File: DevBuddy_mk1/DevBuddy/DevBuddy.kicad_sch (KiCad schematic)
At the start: 5 parts, among them U1 RP2354B

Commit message: Hardware changes, ADC and start of power.
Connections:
- net MUX_S2: now reaches U1.1 (GPIO4)
- net UART_TX_MCU: now reaches U1.77 (GPIO0)
- net UART_RX_MCU: now reaches U1.78 (GPIO1)
- net MUX_S0: now reaches U1.79 (GPIO2)
- net MUX_S1: now reaches U1.80 (GPIO3)
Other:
- added sheet ADC_Channels (ADC_Channels.kicad_sch)
- added sheet Power_Supply_1 (Power_Supply_1.kicad_sch)
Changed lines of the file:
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@@
+	(wire
+		(pts
+			(xy 144.78 71.12) (xy 148.59 71.12)
+		)
+		(stroke
+			(width 0)
+			(type default)
+		)
+	)
 	(wire
 		(pts
@@
 	(wire
 		(pts
+			(xy 144.78 76.2) (xy 148.59 76.2)
+		)
+		(stroke
+			(width 0)
+			(type default)
+		)
+	)
+	(wire
+		(pts
+			(xy 144.78 81.28) (xy 148.59 81.28)
+		)
+		(stroke
+			(width 0)
+			(type default)
+		)
+	)
+	(wire
+		(pts
 			(xy 137.16 45.72) (xy 137.16 46.99)
 		)
@@
 	(wire
 		(pts
+			(xy 144.78 78.74) (xy 148.59 78.74)
+		)
+		(stroke
+			(width 0)
+			(type default)
+		)
+	)
+	(wire
+		(pts
+			(xy 144.78 73.66) (xy 148.59 73.66)
+		)
+		(stroke
+			(width 0)
+			(type default)
+		)
+	)
+	(wire
+		(pts
 			(xy 76.2 44.45) (xy 60.96 44.45)
 		)
@@
 			(width 0)
 			(type default)
+		)
+	)
+	(label "UART_RX_MCU"
+		(at 148.59 73.66 0)
+		(effects
+			(font
+				(size 1.27 1.27)
+			)
+			(justify left bottom)
+		)
+	)
+	(label "UART_TX_MCU"
+		(at 148.59 71.12 0)
+		(effects
+			(font
+				(size 1.27 1.27)
+			)
+			(justify left bottom)
+		)
+	)
+	(global_label "MUX_S1"
+		(shape input)
+		(at 148.59 78.74 0)
+		(fields_autoplaced yes)
+		(effects
+			(font
+				(size 1.27 1.27)
+			)
+			(justify left)
+		)
+		(property "Intersheetrefs" "${INTERSHEET_REFS}"
+			(at 158.9532 78.74 0)
+			(effects
+				(font
+					(size 1.27 1.27)
+				)
+				(justify left)
+				(hide yes)
+			)
+		)
+	)
+	(global_label "MUX_S2"
+		(shape input)
+		(at 148.59 81.28 0)
+		(fields_autoplaced yes)
+		(effects
+			(font
+				(size 1.27 1.27)
+			)
+			(justify left)
+		)
+		(property "Intersheetrefs" "${INTERSHEET_REFS}"
+			(at 158.9532 81.28 0)
+			(effects
+				(font
+					(size 1.27 1.27)
+				)
+				(justify left)
+				(hide yes)
+			)
+		)
+	)
+	(global_label "MUX_S0"
+		(shape input)
+		(at 148.59 76.2 0)
+		(fields_autoplaced yes)
+		(effects
+			(font
+				(size 1.27 1.27)
+			)
+			(justify left)
+		)
+		(property "Intersheetrefs" "${INTERSHEET_REFS}"
+			(at 158.9532 76.2 0)
+			(effects
+				(font
+					(size 1.27 1.27)
+				)
+				(justify left)
+				(hide yes)
+			)
 		)
 	)
@@
 				)
 			)
+		)
+	)
+	(sheet
+		(at 185.42 41.91)
+		(size 57.15 22.86)
+		(exclude_from_sim no)
+		(in_bom yes)
+		(on_board yes)
+		(dnp no)
+		(fields_autoplaced yes)
+		(stroke
+			(width 0.1524)
+			(type solid)
+		)
+		(fill
+			(color 0 0 0 0.0000)
+		)
+		(property "Sheetname" "Power_Supply_1"
+			(at 185.42 41.1984 0)
+			(effects
+				(font
+					(size 1.27 1.27)
+				)
+				(justify left bottom)
+			)
+		)
+		(property "Sheetfile" "Power_Supply_1.kicad_sch"
+			(at 185.42 65.3546 0)
+			(effects
+				(font
+					(size 1.27 1.27)
+				)
+				(justify left top)
+			)
+		)
+		(instances
+			(project "DevBuddy"
+				(path "/cd44a09a-8e2e-49d9-bb56-7efc0bfafbd6"
+					(page "2")
+				)
+			)
+		)
+	)
+	(sheet
+		(at 248.92 41.91)
+		(size 58.42 21.59)
+		(exclude_from_sim no)
+		(in_bom yes)
+		(on_board yes)
+		(dnp no)
+		(fields_autoplaced yes)
+		(stroke
+			(width 0.1524)
+			(type solid)
+		)
+		(fill
+			(color 0 0 0 0.0000)
+		)
+		(property "Sheetname" "ADC_Channels"
+			(at 248.92 41.1984 0)
+			(effects
+				(font
+					(size 1.27 1.27)
+				)
+				(justify left bottom)
+			)
+		)
+		(property "Sheetfile" "ADC_Channels.kicad_sch"
+			(at 248.92 64.0846 0)
+			(effects
+				(font
+					(size 1.27 1.27)
+				)
+				(justify left top)
+			)
+		)
+		(instances
+			(project "DevBuddy"
+				(path "/cd44a09a-8e2e-49d9-bb56-7efc0bfafbd6"
+					(page "3")
+				)
+			)

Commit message: Added mux control, fixed adc tlm control, fixed app, added power in PCB
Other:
- added sheet Power_Supply_2 (Power_Supply_2.kicad_sch)
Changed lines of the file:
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@@
+	)
+	(sheet
+		(at 185.42 73.66)
+		(size 57.15 22.86)
+		(exclude_from_sim no)
+		(in_bom yes)
+		(on_board yes)
+		(dnp no)
+		(fields_autoplaced yes)
+		(stroke
+			(width 0.1524)
+			(type solid)
+		)
+		(fill
+			(color 0 0 0 0.0000)
+		)
+		(property "Sheetname" "Power_Supply_2"
+			(at 185.42 72.9484 0)
+			(effects
+				(font
+					(size 1.27 1.27)
+				)
+				(justify left bottom)
+			)
+		)
+		(property "Sheetfile" "Power_Supply_2.kicad_sch"
+			(at 185.42 97.1046 0)
+			(effects
+				(font
+					(size 1.27 1.27)
+				)
+				(justify left top)
+			)
+		)
+		(instances
+			(project "DevBuddy"
+				(path "/cd44a09a-8e2e-49d9-bb56-7efc0bfafbd6"
+					(page "4")
+				)
+			)
+		)
 	)
 	(sheet

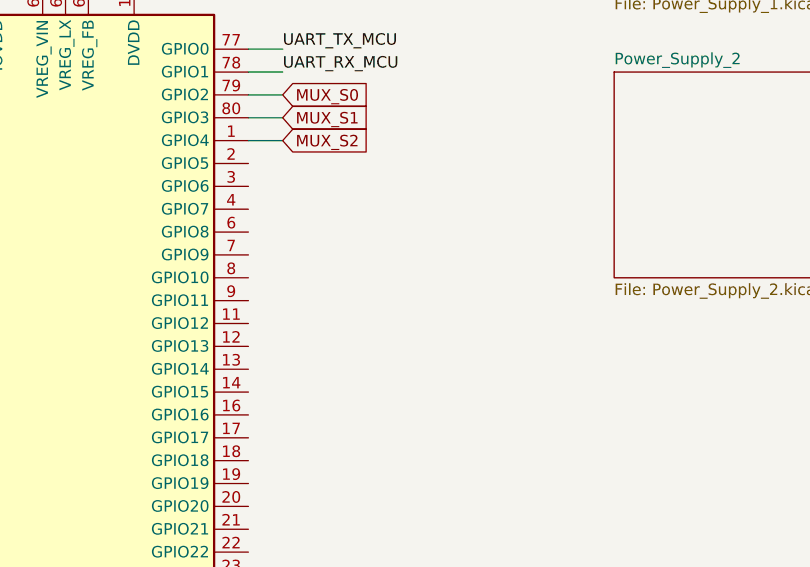
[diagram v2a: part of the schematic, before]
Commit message: Changes in Variable buck - Hardware
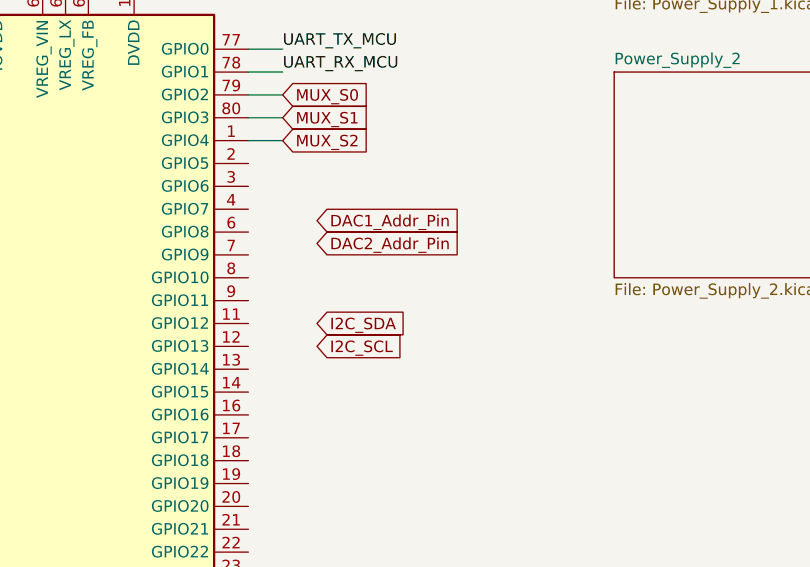
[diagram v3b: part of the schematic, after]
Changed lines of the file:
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@@
+		)
+	)
+	(global_label "DAC1_Addr_Pin"
+		(shape input)
+		(at 152.4 90.17 0)
+		(fields_autoplaced yes)
+		(effects
+			(font
+				(size 1.27 1.27)
+			)
+			(justify left)
+		)
+		(property "Intersheetrefs" "${INTERSHEET_REFS}"
+			(at 169.3551 90.17 0)
+			(effects
+				(font
+					(size 1.27 1.27)
+				)
+				(justify left)
+				(hide yes)
+			)
+		)
+	)
+	(global_label "I2C_SDA"
+		(shape input)
+		(at 152.4 101.6 0)
+		(fields_autoplaced yes)
+		(effects
+			(font
+				(size 1.27 1.27)
+			)
+			(justify left)
+		)
+		(property "Intersheetrefs" "${INTERSHEET_REFS}"
+			(at 163.0052 101.6 0)
+			(effects
+				(font
+					(size 1.27 1.27)
+				)
+				(justify left)
+				(hide yes)
+			)
+		)
+	)
+	(global_label "I2C_SCL"
+		(shape input)
+		(at 152.4 104.14 0)
+		(fields_autoplaced yes)
+		(effects
+			(font
+				(size 1.27 1.27)
+			)
+			(justify left)
+		)
+		(property "Intersheetrefs" "${INTERSHEET_REFS}"
+			(at 162.9447 104.14 0)
+			(effects
+				(font
+					(size 1.27 1.27)
+				)
+				(justify left)
+				(hide yes)
+			)
 		)
 	)
@@
 			(effects
 				(font
+					(size 1.27 1.27)
+				)
+				(justify left)
+				(hide yes)
+			)
+		)
+	)
+	(global_label "DAC2_Addr_Pin"
+		(shape input)
+		(at 152.4 92.71 0)
+		(fields_autoplaced yes)
+		(effects
+			(font
+				(size 1.27 1.27)
+			)
+			(justify left)
+		)
+		(property "Intersheetrefs" "${INTERSHEET_REFS}"
+			(at 169.3551 92.71 0)
+			(effects
+				(font

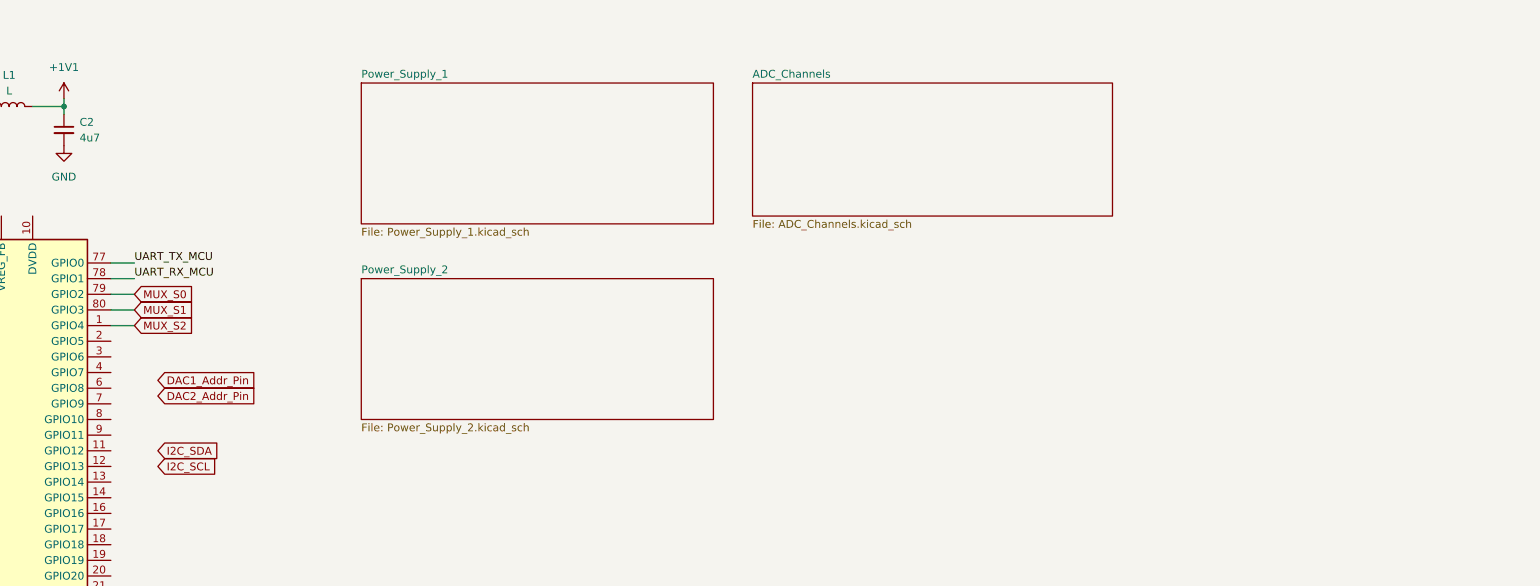
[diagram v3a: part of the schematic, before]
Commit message: Added variable voltage channels/ PCB
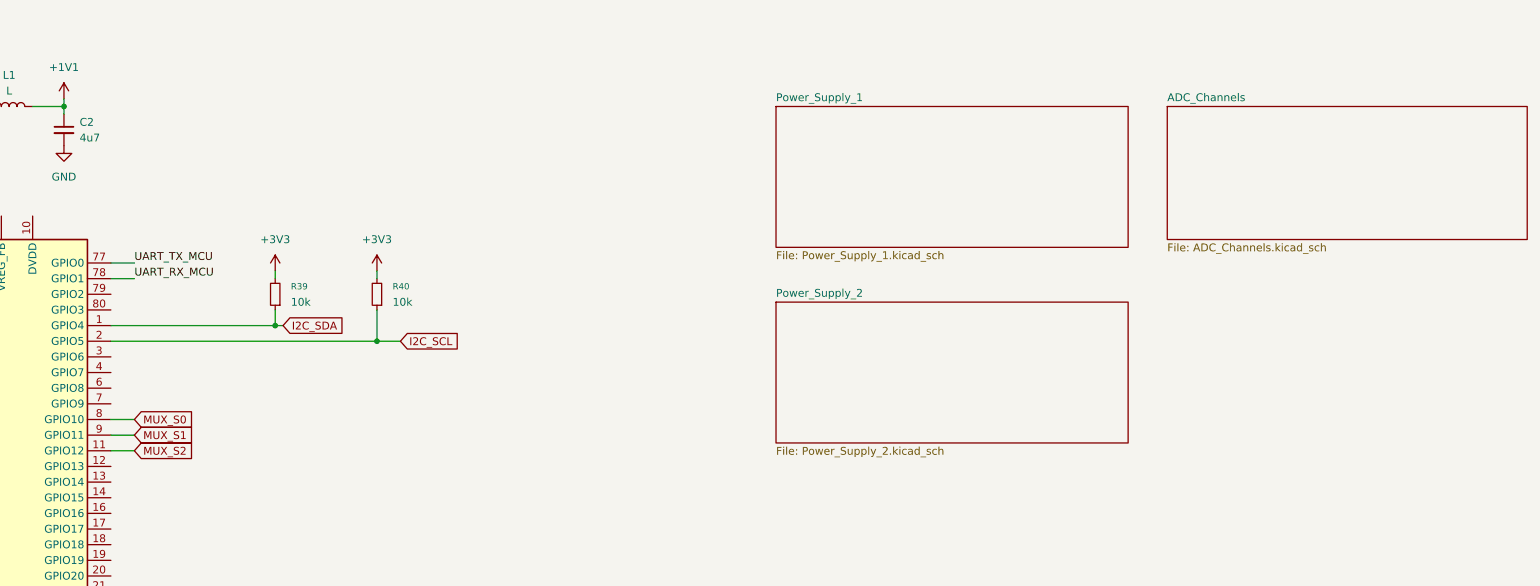
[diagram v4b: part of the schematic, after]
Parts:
- added R39, R40: 10k, Resistor_SMD:R_0402_1005Metric, symbol Device:R_Small
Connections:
- net +3V3: now also R39.2, R40.2
- net I2C_SCL: now also U1.2 (GPIO5), R40.1
- net I2C_SDA: now also U1.1 (GPIO4), R39.1
- net MUX_S0: now also U1.8 (GPIO10); no longer U1.79 (GPIO2)
- net MUX_S1: now also U1.9 (GPIO11); no longer U1.80 (GPIO3)
- net MUX_S2: now also U1.11 (GPIO12); no longer U1.1 (GPIO4)

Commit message: Heavy additions to schematic
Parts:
- removed C1, C2: 4u7, Capacitor_SMD:C_0402_1005Metric, symbol Device:C_Small
- removed L1: L, Inductor_SMD:L_Coilcraft_0805HQ_2012Metric, symbol Device:L
- removed R1: 33R, Resistor_SMD:R_0402_1005Metric, symbol Device:R_Small
- removed R39, R40: 10k, Resistor_SMD:R_0402_1005Metric, symbol Device:R_Small
- removed U1: RP2354B, Package_DFN_QFN:QFN-80-1EP_10x10mm_P0.4mm_EP3.4x3.4mm, symbol MCU_RaspberryPi:RP2354B
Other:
- added sheet DevBuddy_Logic (DevBuddy_Logic.kicad_sch)
- note added: "DevBuddy Mk1"

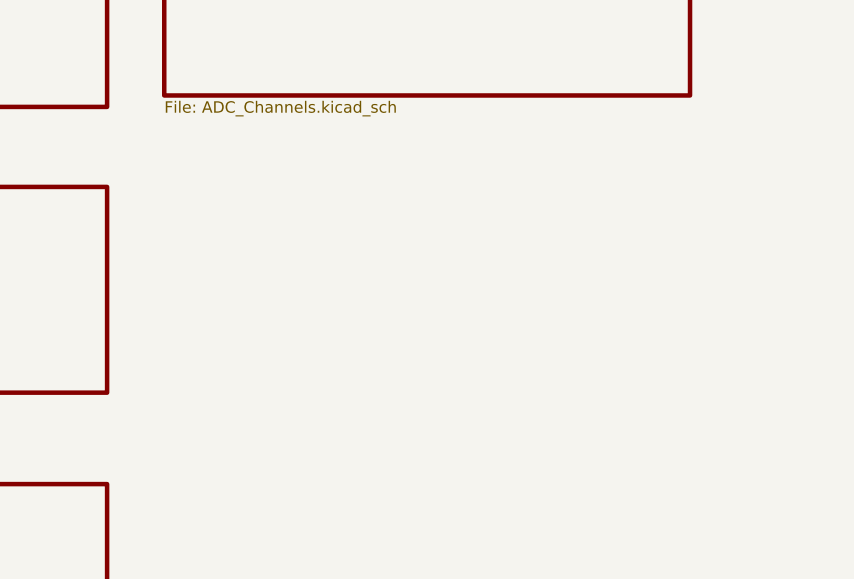
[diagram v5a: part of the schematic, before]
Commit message: More work into the PCB, mainly connectors
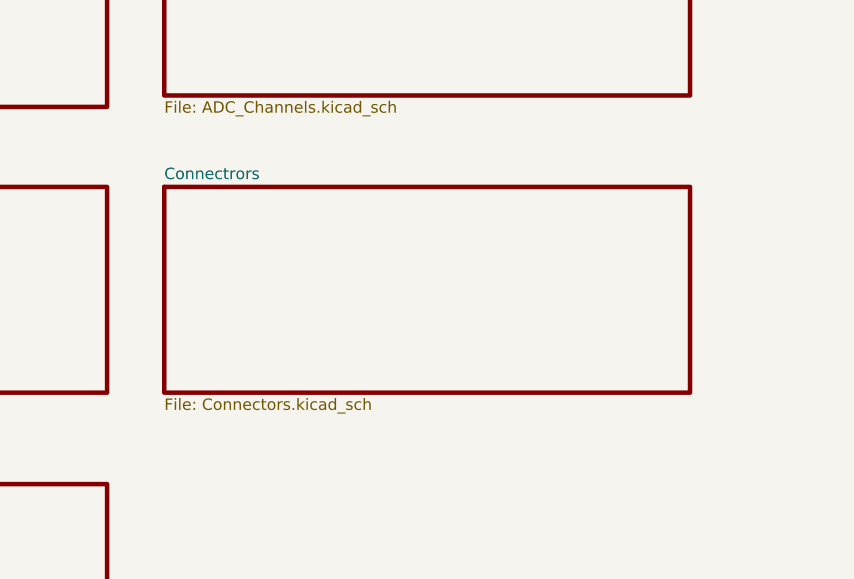
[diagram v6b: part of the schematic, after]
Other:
- added sheet Connectrors (Connectors.kicad_sch)
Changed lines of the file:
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@@
+	)
+	(sheet
+		(at 111.76 76.2)
+		(size 58.42 22.86)
+		(exclude_from_sim no)
+		(in_bom yes)
+		(on_board yes)
+		(dnp no)
+		(fields_autoplaced yes)
+		(stroke
+			(width 0.5)
+			(type solid)
+		)
+		(fill
+			(color 0 0 0 0.0000)
+		)
+		(property "Sheetname" "Connectrors"
+			(at 111.76 75.4884 0)
+			(effects
+				(font
+					(size 1.27 1.27)
+				)
+				(justify left bottom)
+			)
+		)
+		(property "Sheetfile" "Connectors.kicad_sch"
+			(at 111.76 99.6446 0)
+			(effects
+				(font
+					(size 1.27 1.27)
+				)
+				(justify left top)
+			)
+		)
+		(property "Field2" ""
+			(at 111.76 76.2 0)
+			(effects
+				(font
+					(size 1.27 1.27)
+				)
+			)
+		)
+		(instances
+			(project "DevBuddy"
+				(path "/cd44a09a-8e2e-49d9-bb56-7efc0bfafbd6"
+					(page "6")
+				)
+			)
+		)
 	)
 	(sheet
